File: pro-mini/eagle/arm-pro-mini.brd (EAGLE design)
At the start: 38.1 x 20.3 mm, 61 parts, among them J1 MICRO USB, J2 SWD HEADER, Q1 12Mhz, T1 MMBT3906, U1 PRTR5V0U2X, U2 MIC5225-3.3v, U3 LPC11U35FHI33/501, U4 BAS40-05

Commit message: Change the value of R12 (blue led) from 1.5k to 10k. It was too bright.
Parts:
- R12: value 1K5 -> 10K
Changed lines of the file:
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@@
 <attribute name="VALUE" x="17.0688" y="18.161" size="1.27" layer="27" rot="R180"/>
 </element>
-<element name="R12" library="arm-pro-mini" package="R0402" value="1K5" x="16.256" y="14.3764" smashed="yes" rot="R270">
+<element name="R12" library="arm-pro-mini" package="R0402" value="10K" x="16.256" y="14.3764" smashed="yes" rot="R270">
 <attribute name="NAME" x="17.8054" y="13.2334" size="0.8128" layer="25" font="vector" ratio="10" rot="R180"/>
 <attribute name="VALUE" x="14.351" y="15.0114" size="1.27" layer="27" rot="R270"/>

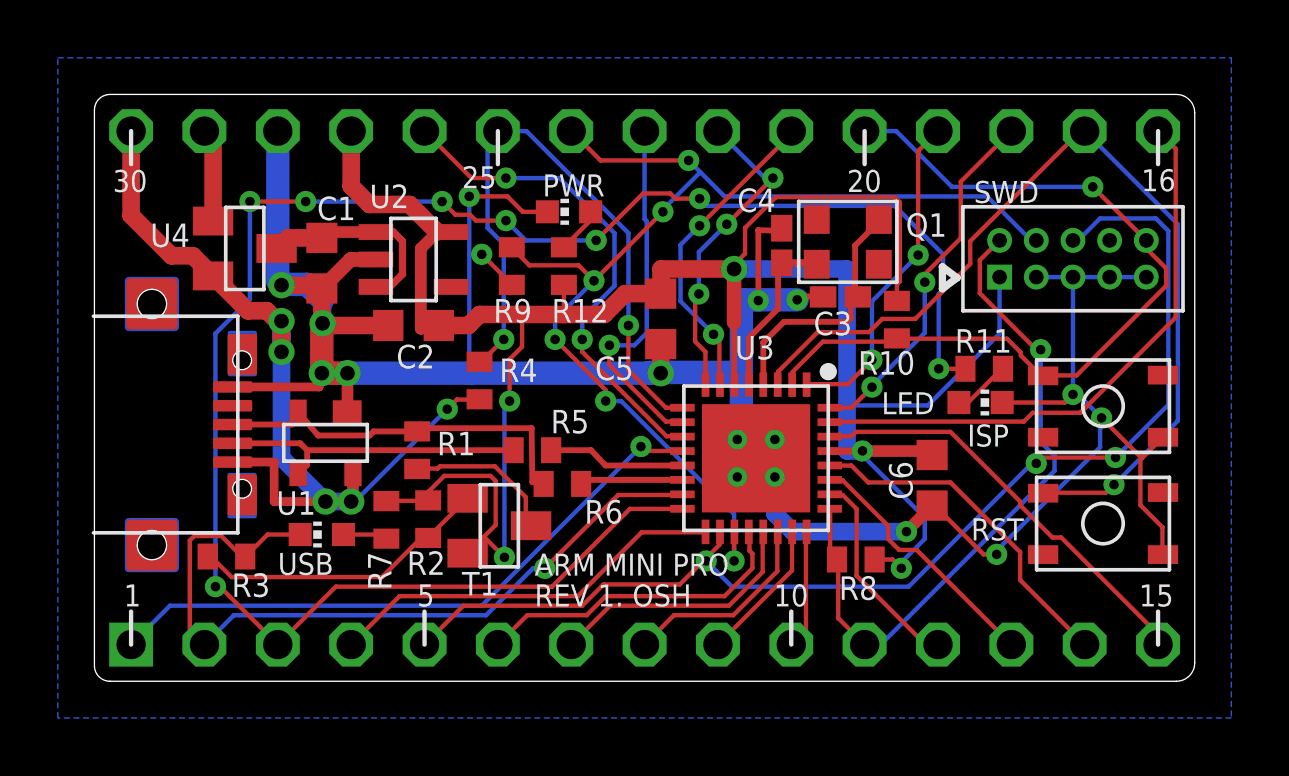
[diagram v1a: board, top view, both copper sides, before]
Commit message: Fixed location of RST and ISP switches labels (were swapped in the layout). Added labels for GND, 5V and 3V3 pins. No semantic change. Made the gerber files obsolete. Will generate new ones.
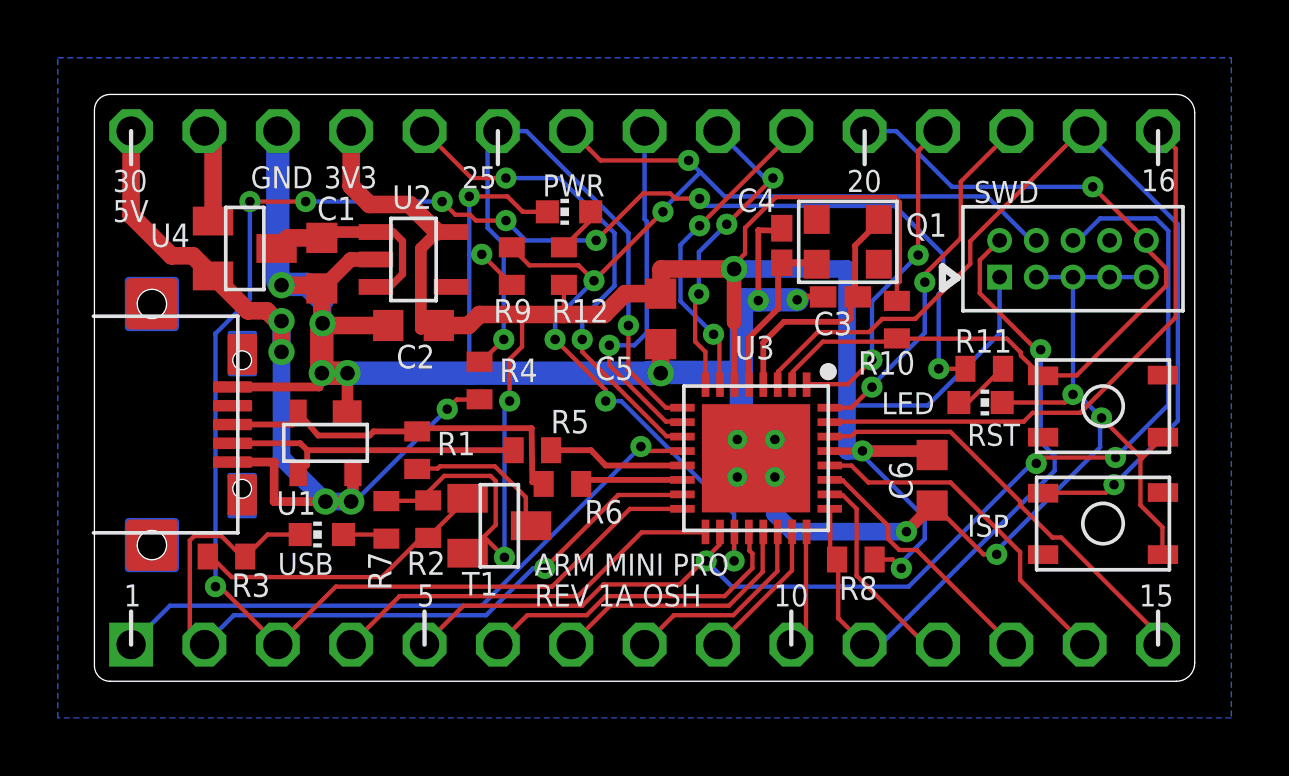
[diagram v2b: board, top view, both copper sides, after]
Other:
- board text added: "3V3"
- board text added: "5V"
- board text added: "GND"
- board text added: "REV 1A OSH"
- board text removed: "REV 1. OSH"
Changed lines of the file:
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@@
 <wire x1="0.5388125" y1="0" x2="37.465" y2="0" width="0" layer="20"/>
 <wire x1="37.465" y1="0" x2="38.1" y2="0.635" width="0" layer="20" curve="90"/>
-<text x="30.353" y="4.8768" size="0.762" layer="21" font="vector" ratio="10">RST</text>
-<text x="30.226" y="8.128" size="0.762" layer="21" font="vector" ratio="10">ISP</text>
+<text x="30.226" y="8.1534" size="0.762" layer="21" font="vector" ratio="10">RST</text>
+<text x="30.226" y="5.0038" size="0.762" layer="21" font="vector" ratio="10">ISP</text>
 <text x="15.5194" y="16.7894" size="0.762" layer="21" font="vector" ratio="10">PWR</text>
 <text x="27.2542" y="9.2456" size="0.762" layer="21" font="vector" ratio="10">LED</text>
@@
 <text x="30.4546" y="16.5608" size="0.762" layer="21" font="vector" ratio="10">SWD</text>
 <text x="15.24" y="3.6576" size="0.762" layer="21" font="vector" ratio="10">ARM MINI PRO</text>
-<text x="15.24" y="2.5908" size="0.762" layer="21" font="vector" ratio="10">REV 1. OSH</text>
+<text x="15.24" y="2.5908" size="0.762" layer="21" font="vector" ratio="10">REV 1A OSH</text>
 <wire x1="1.27" y1="2.413" x2="1.27" y2="1.27" width="0.1524" layer="21"/>
 <wire x1="11.43" y1="2.413" x2="11.43" y2="1.27" width="0.1524" layer="21"/>
@@
 <wire x1="13.97" y1="17.907" x2="13.97" y2="19.05" width="0.1524" layer="21"/>
 <wire x1="1.27" y1="17.907" x2="1.27" y2="19.05" width="0.1524" layer="21"/>
+<text x="5.4102" y="17.0688" size="0.762" layer="21" font="vector" ratio="10">GND</text>
+<text x="7.9502" y="17.0688" size="0.762" layer="21" font="vector" ratio="10">3V3</text>
+<text x="0.635" y="15.9004" size="0.762" layer="21" font="vector" ratio="10">5V</text>
 </plain>
 <attributes>
@@
 </element>
 <element name="U2" library="arm-pro-mini" package="SOT25" value="MIC5225-3.3v" x="11.049" y="14.605" smashed="yes" rot="R270">
-<attribute name="NAME" x="9.525" y="16.383" size="0.8128" layer="25" font="vector" ratio="10"/>
+<attribute name="NAME" x="10.3124" y="16.3576" size="0.8128" layer="25" font="vector" ratio="10"/>
 <attribute name="VALUE" x="7.62" y="16.51" size="1.27" layer="27" rot="R270"/>
 </element>

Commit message: Reduced 0402 resistor footprints to 0.5x0.6mm pads and 0.6mm space.
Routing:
- net +3V3: track 83.7 -> 84.3 mm
